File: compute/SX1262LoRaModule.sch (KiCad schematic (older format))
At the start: 28 parts, among them U201 SX1262, U202 PE4259, Y201 TBD

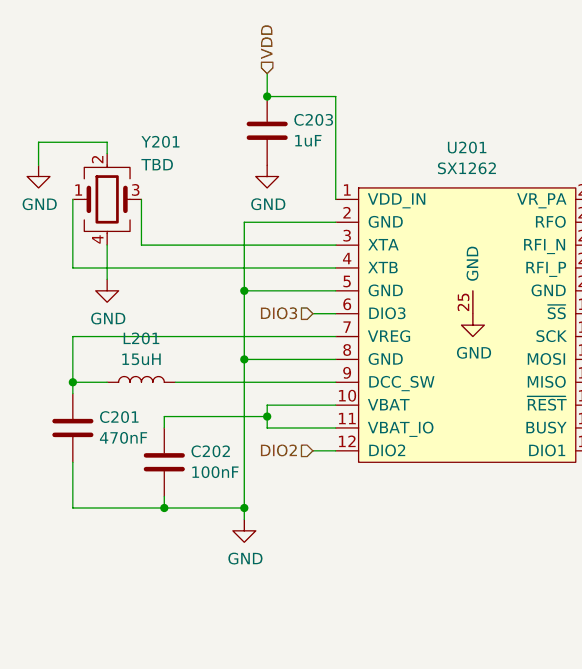
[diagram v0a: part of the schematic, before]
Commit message: Finishing Charge Controller Implementation
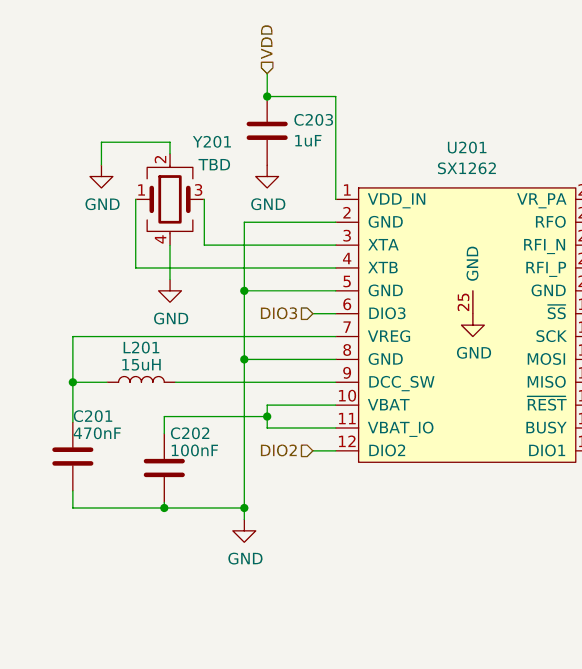
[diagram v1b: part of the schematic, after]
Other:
- moved on the sheet: C201, C202, Y201
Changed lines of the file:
@@
 L Device:C C202
 U 1 1 6189FC21
-P 2900 4350
-F 0 "C202" H 3015 4396 50  0000 L CNN
-F 1 "100nF" H 3015 4305 50  0000 L CNN
-F 2 "Capacitor_SMD:C_0402_1005Metric_Pad0.74x0.62mm_HandSolder" H 2938 4200 50  0001 C CNN
-F 3 "https://www.yageo.com/upload/media/product/productsearch/datasheet/mlcc/UPY-GPHC_X7R_6.3V-to-50V_20.pdf" H 2900 4350 50  0001 C CNN
-F 4 "100nF Capacitor" H 2900 4350 50  0001 C CNN "Description"
-F 5 "Yageo" H 2900 4350 50  0001 C CNN "MFN"
-F 6 "CC0402JRX7R6BB104" H 2900 4350 50  0001 C CNN "MFP"
-F 7 "https://www.digikey.com/en/products/detail/CC0402JRX7R6BB104/311-3757-1-ND/8024846?WT.z_cid=ref_netcomponents_dkc_buynow&utm_source=netcomponents&utm_medium=aggregator&utm_campaign=buynow" H 2900 4350 50  0001 C CNN "S1PL"
-F 8 "311-3757" H 2900 4350 50  0001 C CNN "S1PN"
-F 9 "DNL" H 2900 4350 50  0001 C CNN "Notes"
-	1    2900 4350
+P 2900 4375
+F 0 "C202" H 2925 4525 50  0000 L CNN
+F 1 "100nF" H 2925 4450 50  0000 L CNN
+F 2 "Capacitor_SMD:C_0402_1005Metric_Pad0.74x0.62mm_HandSolder" H 2938 4225 50  0001 C CNN
+F 3 "https://www.yageo.com/upload/media/product/productsearch/datasheet/mlcc/UPY-GPHC_X7R_6.3V-to-50V_20.pdf" H 2900 4375 50  0001 C CNN
+F 4 "100nF Capacitor" H 2900 4375 50  0001 C CNN "Description"
+F 5 "Yageo" H 2900 4375 50  0001 C CNN "MFN"
+F 6 "CC0402JRX7R6BB104" H 2900 4375 50  0001 C CNN "MFP"
+F 7 "https://www.digikey.com/en/products/detail/CC0402JRX7R6BB104/311-3757-1-ND/8024846?WT.z_cid=ref_netcomponents_dkc_buynow&utm_source=netcomponents&utm_medium=aggregator&utm_campaign=buynow" H 2900 4375 50  0001 C CNN "S1PL"
+F 8 "311-3757" H 2900 4375 50  0001 C CNN "S1PN"
+F 9 "DNL" H 2900 4375 50  0001 C CNN "Notes"
+	1    2900 4375
 	1    0    0    -1
 $EndComp
@@
 L Device:C C201
 U 1 1 6189FC27
-P 2500 4200
-F 0 "C201" H 2615 4246 50  0000 L CNN
-F 1 "470nF" H 2615 4155 50  0000 L CNN
-F 2 "Capacitor_SMD:C_0402_1005Metric_Pad0.74x0.62mm_HandSolder" H 2538 4050 50  0001 C CNN
-F 3 "https://www.yageo.com/upload/media/product/productsearch/datasheet/mlcc/UPY-GPHC_X5R_4V-to-50V_27.pdf" H 2500 4200 50  0001 C CNN
-F 4 "470nF Capacitor" H 2500 4200 50  0001 C CNN "Description"
-F 5 "Yageo" H 2500 4200 50  0001 C CNN "MFN"
-F 6 "CC0402KRX5R5BB474" H 2500 4200 50  0001 C CNN "MFP"
-F 7 "http://www.digikey.com/product-detail/en/CC0402KRX5R5BB474/311-1684-1-ND/5195586?WT.z_cid=ref_netcomponents_dkc_buynow&utm_source=netcomponents&utm_medium=aggregator&utm_campaign=buynow" H 2500 4200 50  0001 C CNN "S1PL"
-F 8 "311-1684" H 2500 4200 50  0001 C CNN "S1PN"
-F 9 "https://www.mouser.com/ProductDetail/YAGEO/CC0402KRX5R5BB474?qs=5q%2BqlK8CmJSyt2qjWQmZ1A==&utm_source=netcomponents&utm_medium=aggregator&utm_campaign=CC0402KRX5R5BB474&utm_content=YAGEO" H 2500 4200 50  0001 C CNN "S2PL"
-F 10 "603-CC402KRX5R5BB474" H 2500 4200 50  0001 C CNN "S2PN"
-F 11 "DNL" H 2500 4200 50  0001 C CNN "Notes"
-	1    2500 4200
-	1    0    0    -1
-$EndComp
-Wire Wire Line
-	2500 4000 2500 4050
+P 2500 4325
+F 0 "C201" H 2500 4500 50  0000 L CNN
+F 1 "470nF" H 2500 4425 50  0000 L CNN
+F 2 "Capacitor_SMD:C_0402_1005Metric_Pad0.74x0.62mm_HandSolder" H 2538 4175 50  0001 C CNN
+F 3 "https://www.yageo.com/upload/media/product/productsearch/datasheet/mlcc/UPY-GPHC_X5R_4V-to-50V_27.pdf" H 2500 4325 50  0001 C CNN
+F 4 "470nF Capacitor" H 2500 4325 50  0001 C CNN "Description"
+F 5 "Yageo" H 2500 4325 50  0001 C CNN "MFN"
+F 6 "CC0402KRX5R5BB474" H 2500 4325 50  0001 C CNN "MFP"
+F 7 "http://www.digikey.com/product-detail/en/CC0402KRX5R5BB474/311-1684-1-ND/5195586?WT.z_cid=ref_netcomponents_dkc_buynow&utm_source=netcomponents&utm_medium=aggregator&utm_campaign=buynow" H 2500 4325 50  0001 C CNN "S1PL"
+F 8 "311-1684" H 2500 4325 50  0001 C CNN "S1PN"
+F 9 "https://www.mouser.com/ProductDetail/YAGEO/CC0402KRX5R5BB474?qs=5q%2BqlK8CmJSyt2qjWQmZ1A==&utm_source=netcomponents&utm_medium=aggregator&utm_campaign=CC0402KRX5R5BB474&utm_content=YAGEO" H 2500 4325 50  0001 C CNN "S2PL"
+F 10 "603-CC402KRX5R5BB474" H 2500 4325 50  0001 C CNN "S2PN"
+F 11 "DNL" H 2500 4325 50  0001 C CNN "Notes"
+	1    2500 4325
+	1    0    0    -1
+$EndComp
+Wire Wire Line
+	2500 4000 2500 4175
 Wire Wire Line
 	3650 4100 3350 4100
@@
 	3650 3800 2500 3800
 Wire Wire Line
-	2500 4350 2500 4550
+	2500 4475 2500 4550
 Wire Wire Line
 	2500 4550 2900 4550
@@
 	3250 4550 3250 4600
 Wire Wire Line
-	2900 4500 2900 4550
+	2900 4525 2900 4550
 Connection ~ 2900 4550
 Wire Wire Line
 	2900 4550 3250 4550
 Wire Wire Line
-	2900 4200 2900 4150
+	2900 4225 2900 4150
 Wire Wire Line
 	2900 4150 3350 4150
@@
 L Device:Crystal_GND24 Y201
 U 1 1 619297FF
-P 2650 3200
-F 0 "Y201" H 2800 3450 50  0000 L CNN
-F 1 "TBD" H 2800 3350 50  0000 L CNN
-F 2 "Crystal:Crystal_SMD_2016-4Pin_2.0x1.6mm" H 2650 3200 50  0001 C CNN
-F 3 "~" H 2650 3200 50  0001 C CNN
-F 4 "" H 2650 3200 50  0001 C CNN "MFN"
-F 5 "" H 2650 3200 50  0001 C CNN "MFL"
-F 6 "" H 2650 3200 50  0001 C CNN "S1PN"
-F 7 "" H 2650 3200 50  0001 C CNN "S1PL"
-F 8 "DNL" H 2650 3200 50  0001 C CNN "Notes"
-	1    2650 3200
-	1    0    0    -1
-$EndComp
-Wire Wire Line
-	3650 3400 2800 3400
-Wire Wire Line
-	2800 3400 2800 3200
-Wire Wire Line
-	2500 3200 2500 3500
-Wire Wire Line
-	2500 3500 3650 3500
+P 2925 3200
+F 0 "Y201" H 3025 3450 50  0000 L CNN
+F 1 "TBD" H 3050 3350 50  0000 L CNN
+F 2 "Crystal:Crystal_SMD_2016-4Pin_2.0x1.6mm" H 2925 3200 50  0001 C CNN
+F 3 "~" H 2925 3200 50  0001 C CNN
+F 4 "" H 2925 3200 50  0001 C CNN "MFN"
+F 5 "" H 2925 3200 50  0001 C CNN "MFL"
+F 6 "" H 2925 3200 50  0001 C CNN "S1PN"
+F 7 "" H 2925 3200 50  0001 C CNN "S1PL"
+F 8 "DNL" H 2925 3200 50  0001 C CNN "Notes"
+	1    2925 3200
+	1    0    0    -1
+$EndComp
+Wire Wire Line
+	3075 3400 3075 3200
+Wire Wire Line
+	2775 3200 2775 3500
+Wire Wire Line
+	2775 3500 3650 3500
 $Comp
 L power:GND #PWR0202
 U 1 1 61935D97
-P 2650 3550
-F 0 "#PWR0202" H 2650 3300 50  0001 C CNN
-F 1 "GND" H 2655 3377 50  0000 C CNN
-F 2 "" H 2650 3550 50  0001 C CNN
-F 3 "" H 2650 3550 50  0001 C CNN
-	1    2650 3550
-	1    0    0    -1
-$EndComp
-Wire Wire Line
-	2650 3400 2650 3550
+P 2925 3550
+F 0 "#PWR0202" H 2925 3300 50  0001 C CNN
+F 1 "GND" H 2930 3377 50  0000 C CNN
+F 2 "" H 2925 3550 50  0001 C CNN
+F 3 "" H 2925 3550 50  0001 C CNN
+	1    2925 3550
+	1    0    0    -1
+$EndComp
+Wire Wire Line
+	2925 3400 2925 3550
 $Comp
 L power:GND #PWR0201
 U 1 1 61939540
-P 2350 3050
-F 0 "#PWR0201" H 2350 2800 50  0001 C CNN
-F 1 "GND" H 2355 2877 50  0000 C CNN
-F 2 "" H 2350 3050 50  0001 C CNN
-F 3 "" H 2350 3050 50  0001 C CNN
-	1    2350 3050
-	1    0    0    -1
-$EndComp
-Wire Wire Line
-	2650 3000 2650 2950
-Wire Wire Line
-	2650 2950 2350 2950
-Wire Wire Line
-	2350 2950 2350 3050
+P 2625 3050
+F 0 "#PWR0201" H 2625 2800 50  0001 C CNN
+F 1 "GND" H 2630 2877 50  0000 C CNN
+F 2 "" H 2625 3050 50  0001 C CNN
+F 3 "" H 2625 3050 50  0001 C CNN
+	1    2625 3050
+	1    0    0    -1
+$EndComp
+Wire Wire Line
+	2925 3000 2925 2950
+Wire Wire Line
+	2925 2950 2625 2950
+Wire Wire Line
+	2625 2950 2625 3050
 $Comp
 L power:GND #PWR0205
@@
 U 1 1 6189FC2D
 P 2800 4000
-F 0 "L201" V 2990 4000 50  0000 C CNN
-F 1 "15uH" V 2899 4000 50  0000 C CNN
+F 0 "L201" V 2950 4000 50  0000 C CNN
+F 1 "15uH" V 2875 4000 50  0000 C CNN
 F 2 "Inductor_SMD:L_0805_2012Metric_Pad1.05x1.20mm_HandSolder" H 2800 4000 50  0001 C CNN
 F 3 "~" H 2800 4000 50  0001 C CNN
@@
 	1    0    0    -1
 $EndComp
+Wire Wire Line
+	3650 3400 3075 3400
 $EndSCHEMATC
